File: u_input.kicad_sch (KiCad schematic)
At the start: 21 parts, among them U1 ${SIM.PARAMS}, U3 ${SIM.PARAMS}, U4 ${SIM.PARAMS}, U43 TLV9061xDBV, U5 ${SIM.PARAMS}, U6 ${SIM.PARAMS}, U7 ${SIM.PARAMS}

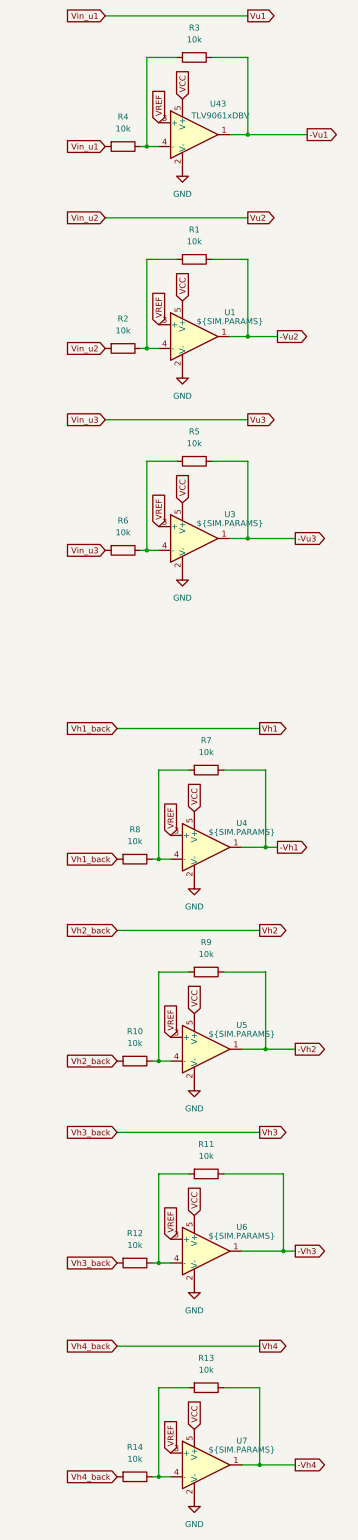
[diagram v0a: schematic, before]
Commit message: Updated: crossbar
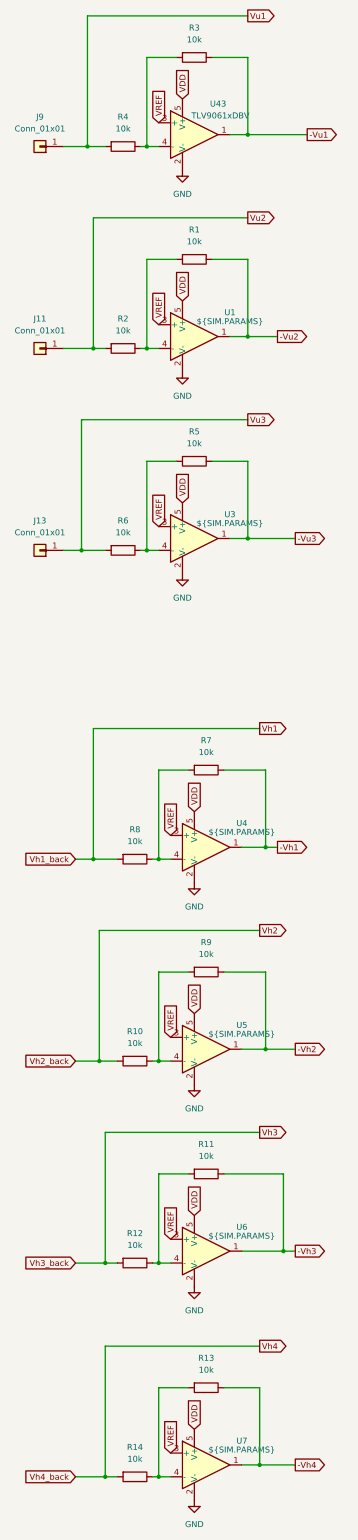
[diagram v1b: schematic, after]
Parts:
- added J11, J13, J9: Conn_01x01, analog_NN:WireSolderPad_1.0mm, symbol Connector_Generic:Conn_01x01
- R1, R10, R11, R12, R13, R14, R2, R3, R4, R5, R6, R7, R8, R9: footprint Resistor_SMD:R_1206_3216Metric_Pad1.30x1.75mm_HandSolder -> Resistor_SMD:R_1206_3216Metric
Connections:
- net VCC renamed VDD
- net Vin_u1 renamed Vu1
- net Vu1: now also J9.1 (Pin_1)
- net Vin_u2 renamed Vu2
- net Vu2: now also J11.1 (Pin_1)
- net Vin_u3 renamed Vu3
- net Vu3: now also J13.1 (Pin_1)

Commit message: Updeated: pcb tracing
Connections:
- net Vu1 renamed +Vu1
- net Vu2 renamed +Vu2
- net Vu3 renamed +Vu3
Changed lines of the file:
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@@
 		)
 	)
-	(global_label "Vu3"
+	(global_label "+Vu3"
 		(shape output)
 		(at 97.79 130.81 0)
@@
 		)
 		(property "Intersheetrefs" "${INTERSHEET_REFS}"
-			(at 104.2223 130.81 0)
+			(at 105.7947 130.81 0)
 			(effects
 				(font
@@
 		)
 	)
-	(global_label "Vu2"
+	(global_label "+Vu2"
 		(shape output)
 		(at 97.79 87.63 0)
@@
 		)
 		(property "Intersheetrefs" "${INTERSHEET_REFS}"
-			(at 104.2223 87.63 0)
+			(at 105.7947 87.63 0)
 			(effects
 				(font
@@
 		)
 	)
-	(global_label "Vu1"
+	(global_label "+Vu1"
 		(shape output)
 		(at 97.79 44.45 0)
@@
 		)
 		(property "Intersheetrefs" "${INTERSHEET_REFS}"
-			(at 104.2223 44.45 0)
+			(at 105.7947 44.45 0)
 			(effects
 				(font

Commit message: Updated: PCB
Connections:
- net Vh1 renamed Vh1_back
- net Vh2 renamed Vh2_back
- net Vh3 renamed Vh3_back
- net Vh4 renamed Vh4_back
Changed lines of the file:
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@@
 	(paper "A3" portrait)
 	(junction
-		(at 64.77 224.79)
-		(diameter 0)
-		(color 0 0 0 0)
-	)
-	(junction
 		(at 76.2 72.39)
 		(diameter 0)
@@
 	)
 	(junction
-		(at 66.04 267.97)
-		(diameter 0)
-		(color 0 0 0 0)
-	)
-	(junction
 		(at 78.74 224.79)
 		(diameter 0)
@@
 	)
 	(junction
-		(at 67.31 356.87)
-		(diameter 0)
-		(color 0 0 0 0)
-	)
-	(junction
 		(at 76.2 115.57)
 		(diameter 0)
@@
 	)
 	(junction
-		(at 67.31 311.15)
-		(diameter 0)
-		(color 0 0 0 0)
-	)
-	(junction
 		(at 100.33 354.33)
 		(diameter 0)
@@
 	(wire
 		(pts
-			(xy 67.31 356.87) (xy 69.85 356.87)
+			(xy 60.96 356.87) (xy 69.85 356.87)
 		)
 		(stroke
@@
 	(wire
 		(pts
-			(xy 60.96 224.79) (xy 64.77 224.79)
-		)
-		(stroke
-			(width 0)
-			(type default)
-		)
-	)
-	(wire
-		(pts
-			(xy 67.31 283.21) (xy 100.33 283.21)
-		)
-		(stroke
-			(width 0)
-			(type default)
-		)
-	)
-	(wire
-		(pts
 			(xy 78.74 248.92) (xy 78.74 267.97)
 		)
@@
 	(wire
 		(pts
-			(xy 60.96 311.15) (xy 67.31 311.15)
-		)
-		(stroke
-			(width 0)
-			(type default)
-		)
-	)
-	(wire
-		(pts
 			(xy 63.5 44.45) (xy 97.79 44.45)
 		)
@@
 	(wire
 		(pts
-			(xy 67.31 283.21) (xy 67.31 311.15)
-		)
-		(stroke
-			(width 0)
-			(type default)
-		)
-	)
-	(wire
-		(pts
 			(xy 76.2 53.34) (xy 76.2 72.39)
 		)
@@
 	(wire
 		(pts
-			(xy 64.77 224.79) (xy 69.85 224.79)
+			(xy 60.96 224.79) (xy 69.85 224.79)
 		)
 		(stroke
@@
 	(wire
 		(pts
-			(xy 67.31 311.15) (xy 69.85 311.15)
-		)
-		(stroke
-			(width 0)
-			(type default)
-		)
-	)
-	(wire
-		(pts
-			(xy 64.77 196.85) (xy 100.33 196.85)
+			(xy 60.96 311.15) (xy 69.85 311.15)
 		)
 		(stroke
@@
 	(wire
 		(pts
-			(xy 60.96 267.97) (xy 66.04 267.97)
+			(xy 60.96 267.97) (xy 69.85 267.97)
 		)
 		(stroke
@@
 	(wire
 		(pts
-			(xy 66.04 267.97) (xy 69.85 267.97)
-		)
-		(stroke
-			(width 0)
-			(type default)
-		)
-	)
-	(wire
-		(pts
 			(xy 101.6 265.43) (xy 107.95 265.43)
 		)
@@
 	(wire
 		(pts
-			(xy 60.96 356.87) (xy 67.31 356.87)
-		)
-		(stroke
-			(width 0)
-			(type default)
-		)
-	)
-	(wire
-		(pts
 			(xy 78.74 356.87) (xy 81.28 356.87)
 		)
@@
 	(wire
 		(pts
-			(xy 67.31 328.93) (xy 67.31 356.87)
-		)
-		(stroke
-			(width 0)
-			(type default)
-		)
-	)
-	(wire
-		(pts
 			(xy 93.98 113.03) (xy 97.79 113.03)
 		)
@@
 	(wire
 		(pts
-			(xy 67.31 328.93) (xy 100.33 328.93)
-		)
-		(stroke
-			(width 0)
-			(type default)
-		)
-	)
-	(wire
-		(pts
 			(xy 97.79 113.03) (xy 104.14 113.03)
 		)
@@
 	(wire
 		(pts
-			(xy 66.04 240.03) (xy 100.33 240.03)
-		)
-		(stroke
-			(width 0)
-			(type default)
-		)
-	)
-	(wire
-		(pts
 			(xy 92.71 337.82) (xy 100.33 337.82)
 		)
@@
 	(wire
 		(pts
-			(xy 66.04 240.03) (xy 66.04 267.97)
-		)
-		(stroke
-			(width 0)
-			(type default)
-		)
-	)
-	(wire
-		(pts
 			(xy 58.42 115.57) (xy 64.77 115.57)
 		)
@@
 	(wire
 		(pts
-			(xy 64.77 196.85) (xy 64.77 224.79)
-		)
-		(stroke
-			(width 0)
-			(type default)
-		)
-	)
-	(wire
-		(pts
 			(xy 63.5 44.45) (xy 63.5 72.39)
 		)
@@
 				)
 				(justify right)
-				(hide yes)
-			)
-		)
-	)
-	(global_label "Vh1"
-		(shape output)
-		(at 100.33 196.85 0)
-		(fields_autoplaced yes)
-		(effects
-			(font
-				(size 1.27 1.27)
-			)
-			(justify left)
-		)
-		(property "Intersheetrefs" "${INTERSHEET_REFS}"
-			(at 106.7623 196.85 0)
-			(effects
-				(font
-					(size 1.27 1.27)
-				)
-				(justify left)
 				(hide yes)
 			)
@@
 		)
 	)
-	(global_label "Vh4"
-		(shape output)
-		(at 100.33 328.93 0)
-		(fields_autoplaced yes)
-		(effects
-			(font
-				(size 1.27 1.27)
-			)
-			(justify left)
-		)
-		(property "Intersheetrefs" "${INTERSHEET_REFS}"
-			(at 106.7623 328.93 0)
-			(effects
-				(font
-					(size 1.27 1.27)
-				)
-				(justify left)
-				(hide yes)
-			)
-		)
-	)
 	(global_label "VREF"
 		(shape input)
@@
 		)
 	)
-	(global_label "Vh3"
-		(shape output)
-		(at 100.33 283.21 0)
-		(fields_autoplaced yes)
-		(effects
-			(font
-				(size 1.27 1.27)
-			)
-			(justify left)
-		)
-		(property "Intersheetrefs" "${INTERSHEET_REFS}"
-			(at 106.7623 283.21 0)
-			(effects
-				(font
-					(size 1.27 1.27)
-				)
-				(justify left)
-				(hide yes)
-			)
-		)
-	)
 	(global_label "-Vu2"
 		(shape output)
@@
 			(effects
 				(font
-					(size 1.27 1.27)
-				)
-				(justify left)
-				(hide yes)
-			)
-		)
-	)
-	(global_label "Vh2"
-		(shape output)
-		(at 100.33 240.03 0)
-		(fields_autoplaced yes)
-		(effects
-			(font
-				(size 1.27 1.27)
-			)
-			(justify left)
-		)
-		(property "Intersheetrefs" "${INTERSHEET_REFS}"
-			(at 106.7623 240.03 0)
-			(effects
-				(font
